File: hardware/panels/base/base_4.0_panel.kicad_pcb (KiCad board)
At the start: 2 copper layers, 94.6 x 93 mm, 50 parts, among them IC1 single_pad_smd, IC2 single_pad_smd, J1 Conn 1, J2 Conn 2

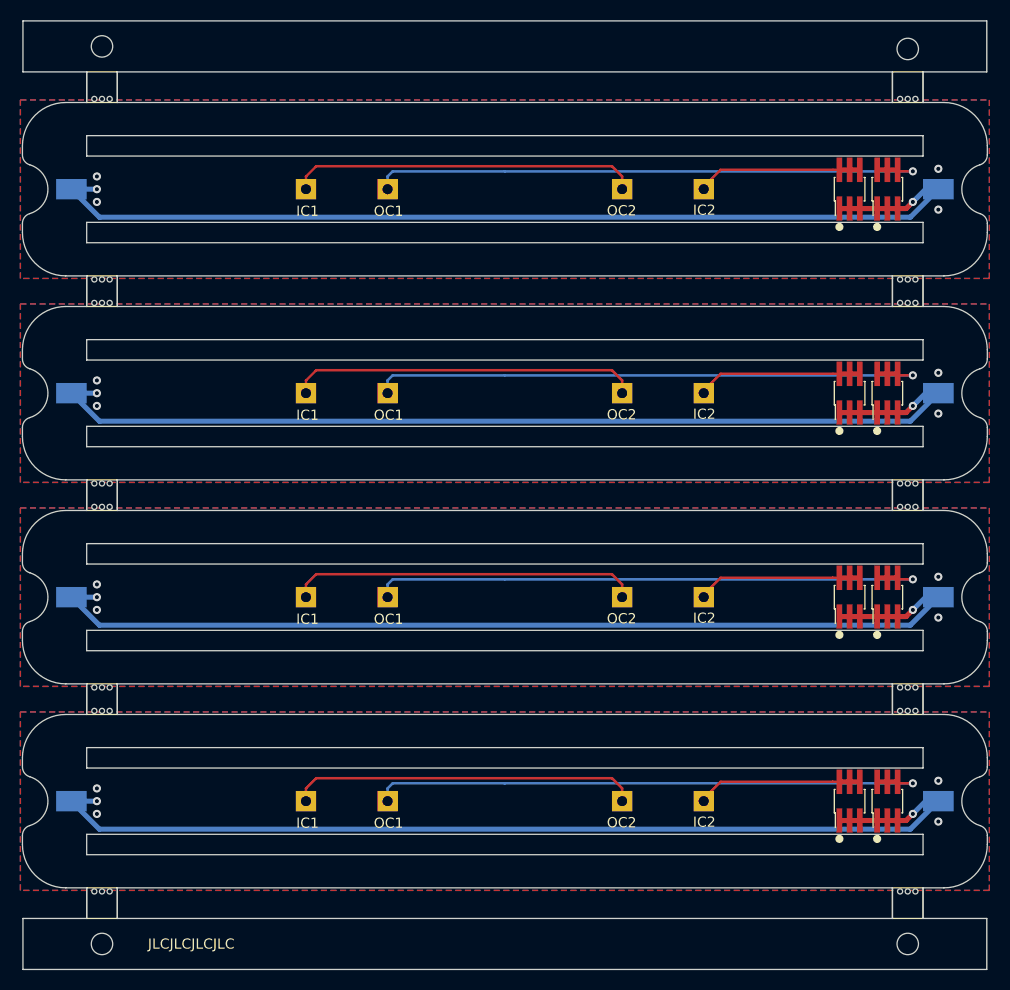
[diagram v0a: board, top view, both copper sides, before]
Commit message: Base PCB panels updates
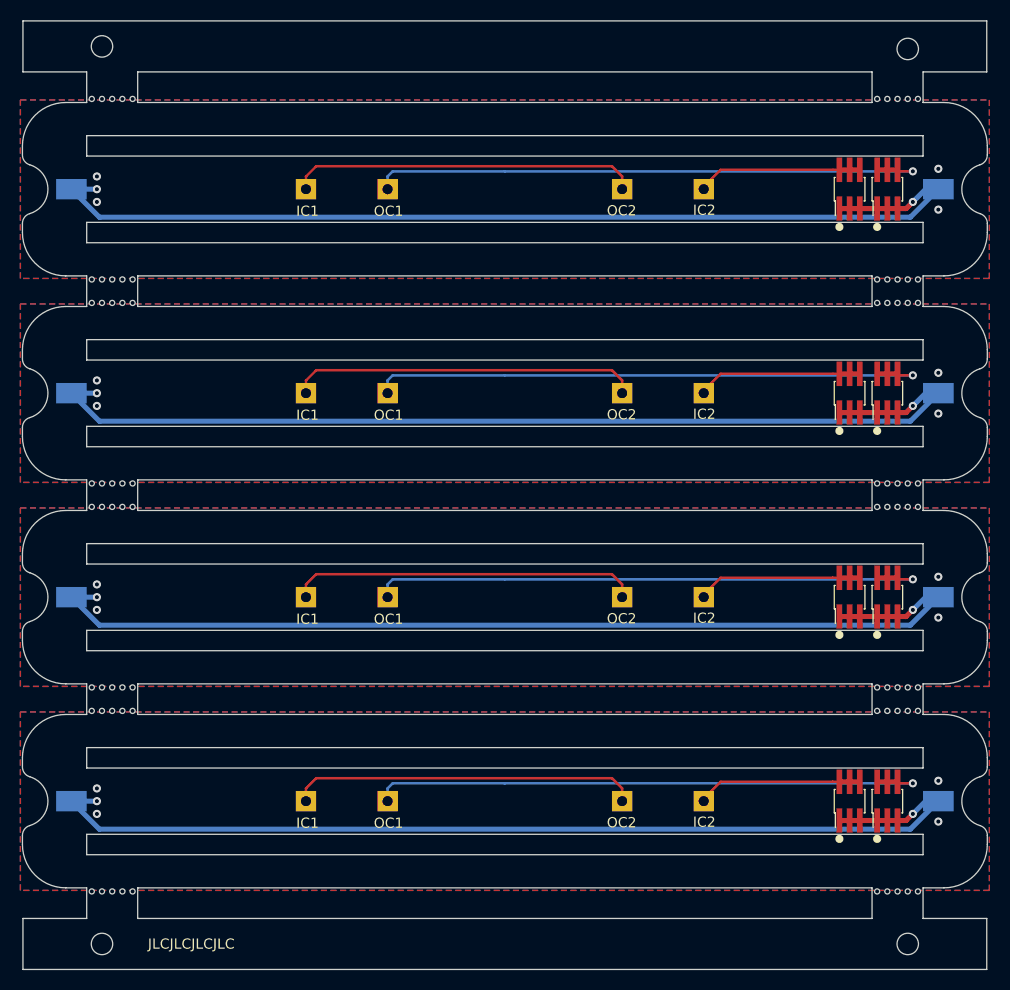
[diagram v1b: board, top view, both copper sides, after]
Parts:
- moved mouse-bite-3mm-slot 1.00 mm to (136.0, 48.5)
- moved mouse-bite-3mm-slot 1.00 mm to (59.0, 68.5)
- moved mouse-bite-3mm-slot 1.00 mm to (59.0, 48.5)
- moved mouse-bite-3mm-slot 1.00 mm to (59.0, 128.5)
- moved mouse-bite-3mm-slot 1.00 mm to (136.0, 128.5)
- moved mouse-bite-3mm-slot 1.00 mm to (136.0, 108.5)
- moved mouse-bite-3mm-slot 1.00 mm to (136.0, 88.5)
- moved mouse-bite-3mm-slot 1.00 mm to (59.0, 108.5)
- moved mouse-bite-3mm-slot 1.00 mm to (59.0, 88.5)
- moved mouse-bite-3mm-slot 1.00 mm to (136.0, 68.5)
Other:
- outline, holes or cut-outs redrawn
